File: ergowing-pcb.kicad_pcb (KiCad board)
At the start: 2 copper layers, 150 parts, among them J1 USB_mini_micro_B, K0:0 KEYSW, K0:1 KEYSW, K0:2 KEYSW, K0:3 KEYSW, K0:4 KEYSW, K10:0 KEYSW, K10:1 KEYSW, K10:2 KEYSW, K10:3 KEYSW, K10:4 KEYSW, K11:0 KEYSW, K11:1 KEYSW, K11:2 KEYSW, K11:3 KEYSW, K11:4 KEYSW, K12:0 KEYSW, K12:1 KEYSW, K12:2 KEYSW, K12:3 KEYSW, K12:4 KEYSW, K13:0 KEYSW, K13:1 KEYSW, K13:2 KEYSW, K13:3 KEYSW, K13:4 KEYSW, K1:0 KEYSW, K1:1 KEYSW, K1:2 KEYSW, K1:3 KEYSW, K1:4 KEYSW, K2:0 KEYSW, K2:1 KEYSW, K2:2 KEYSW, K2:3 KEYSW, K2:4 KEYSW, K3:0 KEYSW, K3:1 KEYSW, K3:2 KEYSW, K3:3 KEYSW, K3:4 KEYSW, K4:0 KEYSW, K4:1 KEYSW, K4:2 KEYSW, K4:3 KEYSW, K4:4 KEYSW, K5:0 KEYSW, K5:1 KEYSW, K5:2 KEYSW, K5:3 KEYSW, K5:4 KEYSW, K6:0 KEYSW, K6:1 KEYSW, K6:3 KEYSW, K7:0 KEYSW, K7:1 KEYSW, K7:3 KEYSW, K7:4 KEYSW, K8:0 KEYSW, K8:1 KEYSW, K8:2 KEYSW, K8:3 KEYSW, K8:4 KEYSW, K9:0 KEYSW, K9:1 KEYSW, K9:2 KEYSW, K9:3 KEYSW, K9:4 KEYSW, SW1 SW_PUSH, U1 ATMEGA32U4, X1 XTAL_GND

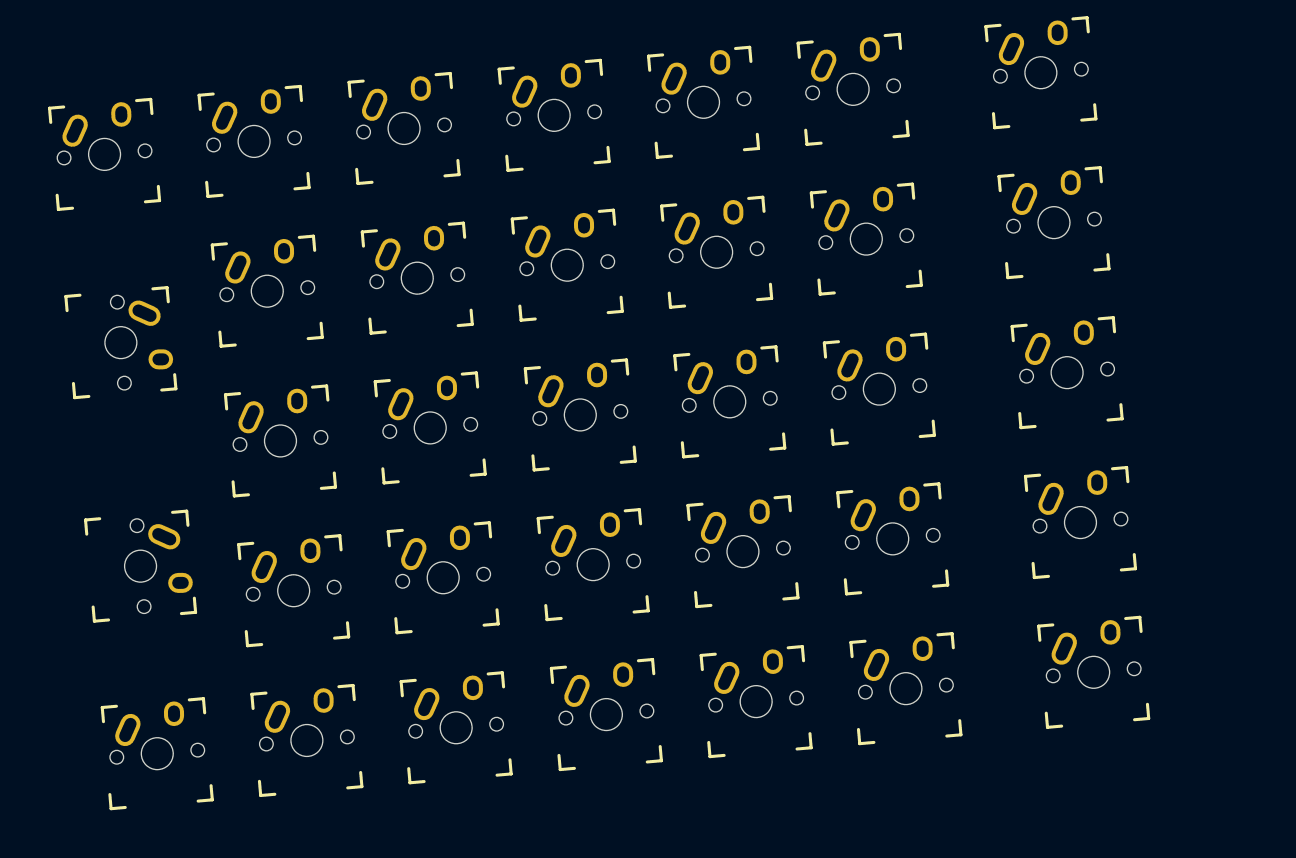
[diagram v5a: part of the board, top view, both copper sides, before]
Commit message: Layout update, left and right are correct distance
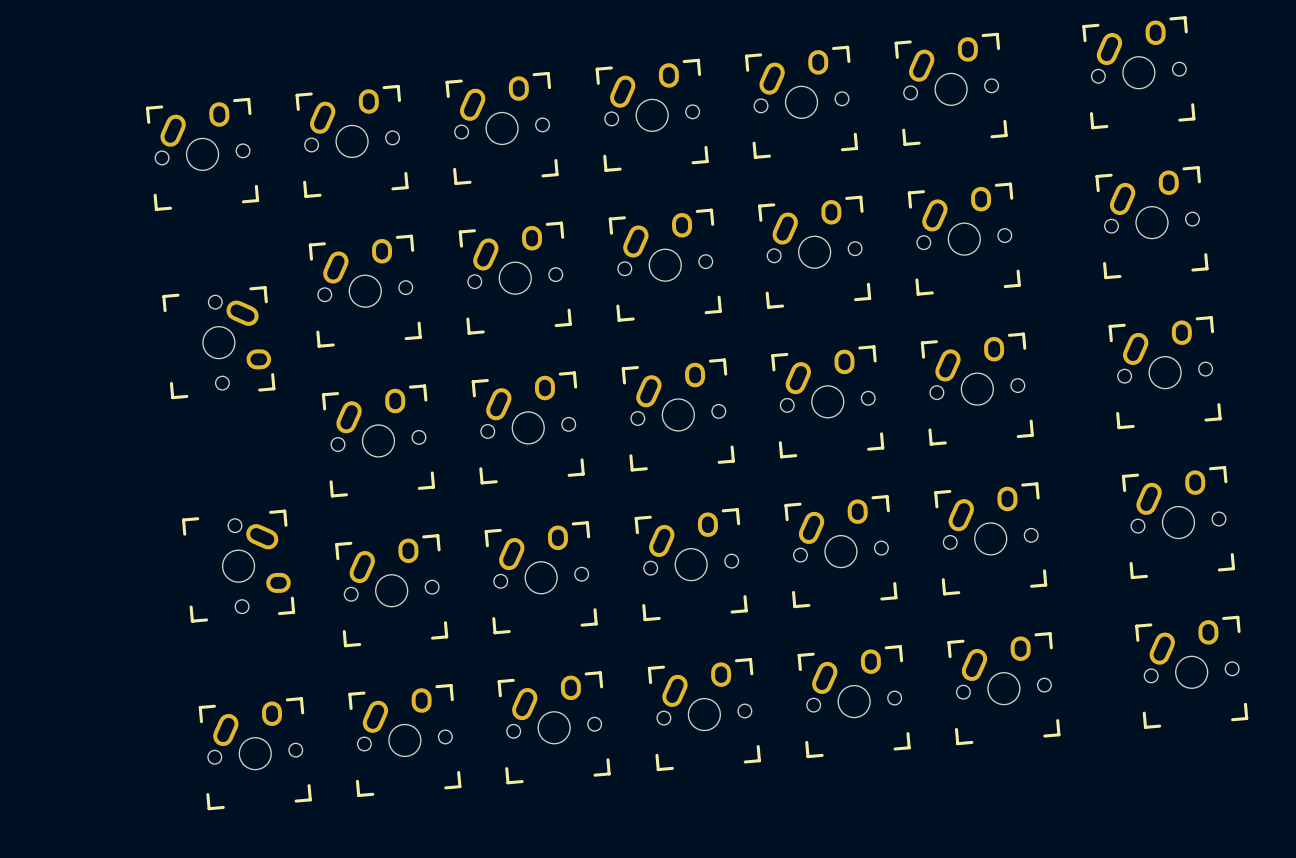
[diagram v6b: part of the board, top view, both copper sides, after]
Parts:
- moved K9:2 12.3 mm to (257.5, 102.9)
- moved K9:4 12.3 mm to (259.2, 121.6)
- moved K10:0 12.2 mm to (271.4, 45.1)
- moved K10:1 12.2 mm to (273.1, 63.8)
- moved K10:2 12.2 mm to (274.7, 82.5)
- moved K10:3 12.2 mm to (276.3, 101.2)
- moved K10:4 12.2 mm to (277.9, 120.0)
- moved K11:0 12.2 mm to (290.1, 43.5)
- moved K11:1 12.2 mm to (291.7, 62.2)
- moved K11:2 12.2 mm to (293.4, 80.9)
- moved K11:3 12.2 mm to (295.0, 99.6)
- moved K11:4 12.2 mm to (296.7, 118.4)
- moved K12:0 12.2 mm to (308.8, 41.8)
- moved K12:1 12.2 mm to (310.4, 60.5)
- moved K12:2 12.2 mm to (312.1, 79.3)
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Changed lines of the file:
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@@
     (pad_to_mask_clearance 0.2)
     (aux_axis_origin 0 0)
+    (grid_origin 12 12)
     (visible_elements 7FFFF7FF)
     (pcbplotparams
@@
   )
   (module keebs:Mx_Alps_150 (layer F.Cu)
-    (at 205 73.49 275)
+    (at 217.25 73.49 275)
     (descr MXALPS)
     (tags MXALPS)
@@
   )
   (module keebs:Mx_Alps_150 (layer F.Cu)
-    (at 207.46 101.43 275)
+    (at 219.71 101.43 275)
     (descr MXALPS)
     (tags MXALPS)
@@
   )
   (module keebs:Mx_Alps_100_R5deg (layer F.Cu)
-    (at 202.96 49.96)
+    (at 215.21 49.96)
     (descr MXALPS)
     (tags MXALPS)
@@
   )
   (module keebs:Mx_Alps_100_R5deg (layer F.Cu)
-    (at 209.55 124.87)
+    (at 221.8 124.87)
     (descr MXALPS)
     (tags MXALPS)
@@
   )
   (module keebs:Mx_Alps_100_R5deg (layer F.Cu)
-    (at 221.65 48.34)
+    (at 233.9 48.34)
     (descr MXALPS)
     (tags MXALPS)
@@
   )
   (module keebs:Mx_Alps_100_R5deg (layer F.Cu)
-    (at 223.3 67.06)
+    (at 235.55 67.06)
     (descr MXALPS)
     (tags MXALPS)
@@
   )
   (module keebs:Mx_Alps_100_R5deg (layer F.Cu)
-    (at 224.95 85.78)
+    (at 237.2 85.78)
     (descr MXALPS)
     (tags MXALPS)
@@
   )
   (module keebs:Mx_Alps_100_R5deg (layer F.Cu)
-    (at 226.6 104.5)
+    (at 238.85 104.5)
     (descr MXALPS)
     (tags MXALPS)
@@
   )
   (module keebs:Mx_Alps_100_R5deg (layer F.Cu)
-    (at 228.25 123.22)
+    (at 240.5 123.22)
     (descr MXALPS)
     (tags MXALPS)
@@
   )
   (module keebs:Mx_Alps_100_R5deg (layer F.Cu)
-    (at 240.4 46.72)
+    (at 252.65 46.72)
     (descr MXALPS)
     (tags MXALPS)
@@
   )
   (module keebs:Mx_Alps_100_R5deg (layer F.Cu)
-    (at 242.05 65.43)
+    (at 254.3 65.43)
     (descr MXALPS)
     (tags MXALPS)
@@
   )
   (module keebs:Mx_Alps_100_R5deg (layer F.Cu)
-    (at 245.29 102.88)
+    (at 257.54 102.88)
     (descr MXALPS)
     (tags MXALPS)
@@
   )
   (module keebs:Mx_Alps_100_R5deg (layer F.Cu)
-    (at 243.67 84.15)
+    (at 255.92 84.15)
     (descr MXALPS)
     (tags MXALPS)
@@
   )
   (module keebs:Mx_Alps_100_R5deg (layer F.Cu)
-    (at 246.91 121.63)
+    (at 259.16 121.63)
     (descr MXALPS)
     (tags MXALPS)
@@
   )
   (module keebs:Mx_Alps_100_R5deg (layer F.Cu)
-    (at 259.16 45.08)
+    (at 271.41 45.08)
     (descr MXALPS)
     (tags MXALPS)
@@
   )
   (module keebs:Mx_Alps_100_R5deg (layer F.Cu)
-    (at 260.8 63.81)
+    (at 273.05 63.81)
     (descr MXALPS)
     (tags MXALPS)
@@
   )
   (module keebs:Mx_Alps_100_R5deg (layer F.Cu)
-    (at 262.43 82.53)
+    (at 274.68 82.53)
     (descr MXALPS)
     (tags MXALPS)
@@
   )
   (module keebs:Mx_Alps_100_R5deg (layer F.Cu)
-    (at 264.04 101.24)
+    (at 276.29 101.24)
     (descr MXALPS)
     (tags MXALPS)
@@
   )
   (module keebs:Mx_Alps_100_R5deg (layer F.Cu)
-    (at 265.69 119.98)
+    (at 277.94 119.98)
     (descr MXALPS)
     (tags MXALPS)
@@
   )
   (module keebs:Mx_Alps_100_R5deg (layer F.Cu)
-    (at 277.83 43.45)
+    (at 290.08 43.45)
     (descr MXALPS)
     (tags MXALPS)
@@
   )
   (module keebs:Mx_Alps_100_R5deg (layer F.Cu)
-    (at 279.47 62.19)
+    (at 291.72 62.19)
     (descr MXALPS)
     (tags MXALPS)
@@
   )
   (module keebs:Mx_Alps_100_R5deg (layer F.Cu)
-    (at 281.11 80.89)
+    (at 293.36 80.89)
     (descr MXALPS)
     (tags MXALPS)
@@
   )
   (module keebs:Mx_Alps_100_R5deg (layer F.Cu)
-    (at 282.76 99.61)
+    (at 295.01 99.61)
     (descr MXALPS)
     (tags MXALPS)
@@
   )
   (module keebs:Mx_Alps_100_R5deg (layer F.Cu)
-    (at 284.41 118.36)
+    (at 296.66 118.36)
     (descr MXALPS)
     (tags MXALPS)
@@
   )
   (module keebs:Mx_Alps_100_R5deg (layer F.Cu)
-    (at 296.53 41.83)
+    (at 308.78 41.83)
     (descr MXALPS)
     (tags MXALPS)
@@
   )
   (module keebs:Mx_Alps_100_R5deg (layer F.Cu)
-    (at 298.18 60.55)
+    (at 310.43 60.55)
     (descr MXALPS)
     (tags MXALPS)
@@
   )
   (module keebs:Mx_Alps_100_R5deg (layer F.Cu)
-    (at 299.81 79.3)
+    (at 312.06 79.3)
     (descr MXALPS)
     (tags MXALPS)
@@
   )
   (module keebs:Mx_Alps_100_R5deg (layer F.Cu)
-    (at 303.13 116.74)
+    (at 315.38 116.74)
     (descr MXALPS)
     (tags MXALPS)
@@
   )
   (module keebs:Mx_Alps_100_R5deg (layer F.Cu)
-    (at 301.48 98.02)
+    (at 313.73 98.02)
     (descr MXALPS)
     (tags MXALPS)
@@
   )
   (module keebs:Mx_Alps_150_R5deg (layer F.Cu)
-    (at 320 39.75)
+    (at 332.25 39.75)
     (descr MXALPS)
     (tags MXALPS)
@@
   )
   (module keebs:Mx_Alps_150_R5deg (layer F.Cu)
-    (at 321.64 58.49)
+    (at 333.89 58.49)
     (descr MXALPS)
     (tags MXALPS)
@@
   )
   (module keebs:Mx_Alps_150_R5deg (layer F.Cu)
-    (at 323.28 77.24)
+    (at 335.53 77.24)
     (descr MXALPS)
     (tags MXALPS)
@@
   )
   (module keebs:Mx_Alps_150_R5deg (layer F.Cu)
-    (at 324.95 95.98)
+    (at 337.2 95.98)
     (descr MXALPS)
     (tags MXALPS)
@@
   )
   (module keebs:Mx_Alps_150_R5deg (layer F.Cu)
-    (at 326.6 114.7)
+    (at 338.85 114.7)
     (descr MXALPS)
     (tags MXALPS)

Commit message: Update #321312
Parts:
- moved K4:4 7.57 mm to (139.2, 114.1)
- moved K3:4 4.56 mm to (120.2, 115.4)
- moved K3:3 4.56 mm to (121.8, 96.7)
- moved K3:0 4.56 mm to (126.7, 40.5)
- moved K3:1 4.56 mm to (125.1, 59.2)
- moved K3:2 4.56 mm to (123.4, 78.0)
- moved K2:1 3.10 mm to (106.2, 59.0)
- moved K2:3 3.10 mm to (103.0, 96.5)
- moved K2:4 3.10 mm to (101.3, 115.2)
- moved K2:0 3.10 mm to (107.9, 40.3)
- moved K2:2 3.10 mm to (104.6, 77.8)
- moved K4:2 3.01 mm to (142.1, 81.2)
- moved K4:0 3.01 mm to (145.3, 43.7)
- moved K4:1 3.01 mm to (143.7, 62.4)
- moved K4:3 3.01 mm to (140.4, 99.9)
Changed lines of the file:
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@@
     (links 515)
     (no_connects 247)
-    (area 43.748094 28.857392 395.425 379.0775)
+    (area 43.337667 26.864461 395.425 379.0775)
     (thickness 1.6)
     (drawings 0)
@@
   )
   (module keebs:Mx_Alps_100_R-5deg (layer F.Cu)
-    (at 107.63 43.4)
+    (at 107.88 40.31)
     (descr MXALPS)
     (tags MXALPS)
@@
   )
   (module keebs:Mx_Alps_100_R-5deg (layer F.Cu)
-    (at 105.99 62.14)
+    (at 106.24 59.05)
     (descr MXALPS)
     (tags MXALPS)
@@
   )
   (module keebs:Mx_Alps_100_R-5deg (layer F.Cu)
-    (at 104.36 80.85)
+    (at 104.61 77.76)
     (descr MXALPS)
     (tags MXALPS)
@@
   )
   (module keebs:Mx_Alps_100_R-5deg (layer F.Cu)
-    (at 102.72 99.59)
+    (at 102.97 96.5)
     (descr MXALPS)
     (tags MXALPS)
@@
   )
   (module keebs:Mx_Alps_100_R-5deg (layer F.Cu)
-    (at 101.08 118.3)
+    (at 101.33 115.21)
     (descr MXALPS)
     (tags MXALPS)
@@
   )
   (module keebs:Mx_Alps_100_R-5deg (layer F.Cu)
-    (at 126.34 45.03)
+    (at 126.74 40.49)
     (descr MXALPS)
     (tags MXALPS)
@@
   )
   (module keebs:Mx_Alps_100_R-5deg (layer F.Cu)
-    (at 124.7 63.74)
+    (at 125.1 59.2)
     (descr MXALPS)
     (tags MXALPS)
@@
   )
   (module keebs:Mx_Alps_100_R-5deg (layer F.Cu)
-    (at 123.02 82.49)
+    (at 123.42 77.95)
     (descr MXALPS)
     (tags MXALPS)
@@
   )
   (module keebs:Mx_Alps_100_R-5deg (layer F.Cu)
-    (at 121.37 101.2)
+    (at 121.77 96.66)
     (descr MXALPS)
     (tags MXALPS)
@@
   )
   (module keebs:Mx_Alps_100_R-5deg (layer F.Cu)
-    (at 119.75 119.95)
+    (at 120.15 115.41)
     (descr MXALPS)
     (tags MXALPS)
@@
   )
   (module keebs:Mx_Alps_100_R-5deg (layer F.Cu)
-    (at 145.09 46.69)
+    (at 145.32 43.69)
     (descr MXALPS)
     (tags MXALPS)
@@
   )
   (module keebs:Mx_Alps_100_R-5deg (layer F.Cu)
-    (at 143.47 65.41)
+    (at 143.7 62.41)
     (descr MXALPS)
     (tags MXALPS)
@@
   )
   (module keebs:Mx_Alps_100_R-5deg (layer F.Cu)
-    (at 141.85 84.16)
+    (at 142.08 81.16)
     (descr MXALPS)
     (tags MXALPS)
@@
   )
   (module keebs:Mx_Alps_100_R-5deg (layer F.Cu)
-    (at 140.21 102.87)
+    (at 140.44 99.87)
     (descr MXALPS)
     (tags MXALPS)
@@
   )
   (module keebs:Mx_Alps_100_R-5deg (layer F.Cu)
-    (at 138.57 121.62)
+    (at 139.2 114.08)
     (descr MXALPS)
     (tags MXALPS)

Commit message: Revert "Update #321312"
This reverts commit 362bd967889284bfad0d96aa47e5c379ba675c40.
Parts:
- moved K4:4 7.57 mm to (138.6, 121.6)
- moved K3:4 4.56 mm to (119.8, 120.0)
- moved K3:3 4.56 mm to (121.4, 101.2)
- moved K3:0 4.56 mm to (126.3, 45.0)
- moved K3:1 4.56 mm to (124.7, 63.7)
- moved K3:2 4.56 mm to (123.0, 82.5)
- moved K2:1 3.10 mm to (106.0, 62.1)
- moved K2:3 3.10 mm to (102.7, 99.6)
- moved K2:4 3.10 mm to (101.1, 118.3)
- moved K2:0 3.10 mm to (107.6, 43.4)
- moved K2:2 3.10 mm to (104.4, 80.8)
- moved K4:2 3.01 mm to (141.8, 84.2)
- moved K4:0 3.01 mm to (145.1, 46.7)
- moved K4:1 3.01 mm to (143.5, 65.4)
- moved K4:3 3.01 mm to (140.2, 102.9)
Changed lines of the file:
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@@
     (links 515)
     (no_connects 247)
-    (area 43.337667 26.864461 395.425 379.0775)
+    (area 43.748094 28.857392 395.425 379.0775)
     (thickness 1.6)
     (drawings 0)
@@
   )
   (module keebs:Mx_Alps_100_R-5deg (layer F.Cu)
-    (at 107.88 40.31)
+    (at 107.63 43.4)
     (descr MXALPS)
     (tags MXALPS)
@@
   )
   (module keebs:Mx_Alps_100_R-5deg (layer F.Cu)
-    (at 106.24 59.05)
+    (at 105.99 62.14)
     (descr MXALPS)
     (tags MXALPS)
@@
   )
   (module keebs:Mx_Alps_100_R-5deg (layer F.Cu)
-    (at 104.61 77.76)
+    (at 104.36 80.85)
     (descr MXALPS)
     (tags MXALPS)
@@
   )
   (module keebs:Mx_Alps_100_R-5deg (layer F.Cu)
-    (at 102.97 96.5)
+    (at 102.72 99.59)
     (descr MXALPS)
     (tags MXALPS)
@@
   )
   (module keebs:Mx_Alps_100_R-5deg (layer F.Cu)
-    (at 101.33 115.21)
+    (at 101.08 118.3)
     (descr MXALPS)
     (tags MXALPS)
@@
   )
   (module keebs:Mx_Alps_100_R-5deg (layer F.Cu)
-    (at 126.74 40.49)
+    (at 126.34 45.03)
     (descr MXALPS)
     (tags MXALPS)
@@
   )
   (module keebs:Mx_Alps_100_R-5deg (layer F.Cu)
-    (at 125.1 59.2)
+    (at 124.7 63.74)
     (descr MXALPS)
     (tags MXALPS)
@@
   )
   (module keebs:Mx_Alps_100_R-5deg (layer F.Cu)
-    (at 123.42 77.95)
+    (at 123.02 82.49)
     (descr MXALPS)
     (tags MXALPS)
@@
   )
   (module keebs:Mx_Alps_100_R-5deg (layer F.Cu)
-    (at 121.77 96.66)
+    (at 121.37 101.2)
     (descr MXALPS)
     (tags MXALPS)
@@
   )
   (module keebs:Mx_Alps_100_R-5deg (layer F.Cu)
-    (at 120.15 115.41)
+    (at 119.75 119.95)
     (descr MXALPS)
     (tags MXALPS)
@@
   )
   (module keebs:Mx_Alps_100_R-5deg (layer F.Cu)
-    (at 145.32 43.69)
+    (at 145.09 46.69)
     (descr MXALPS)
     (tags MXALPS)
@@
   )
   (module keebs:Mx_Alps_100_R-5deg (layer F.Cu)
-    (at 143.7 62.41)
+    (at 143.47 65.41)
     (descr MXALPS)
     (tags MXALPS)
@@
   )
   (module keebs:Mx_Alps_100_R-5deg (layer F.Cu)
-    (at 142.08 81.16)
+    (at 141.85 84.16)
     (descr MXALPS)
     (tags MXALPS)
@@
   )
   (module keebs:Mx_Alps_100_R-5deg (layer F.Cu)
-    (at 140.44 99.87)
+    (at 140.21 102.87)
     (descr MXALPS)
     (tags MXALPS)
@@
   )
   (module keebs:Mx_Alps_100_R-5deg (layer F.Cu)
-    (at 139.2 114.08)
+    (at 138.57 121.62)
     (descr MXALPS)
     (tags MXALPS)
